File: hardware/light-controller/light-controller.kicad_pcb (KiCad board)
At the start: 2 copper layers, 73 x 35 mm, 124 parts, among them J1 BATT 4S-6S, J2 USB-C, J3 SWD, J4 UART to FC, M1 RM2, Q1 DMP6023LE, SW1 BOOTSEL, U1 LMR51420YDDCR, U2 RP2350A, U3 W25Q16JVSNIQ, U4 USBLC6-2SC6, U5 AL8860MP-13, U6 AL8860MP-13, U7 AL8860MP-13, U8 AL8860MP-13, Y1 12MHz

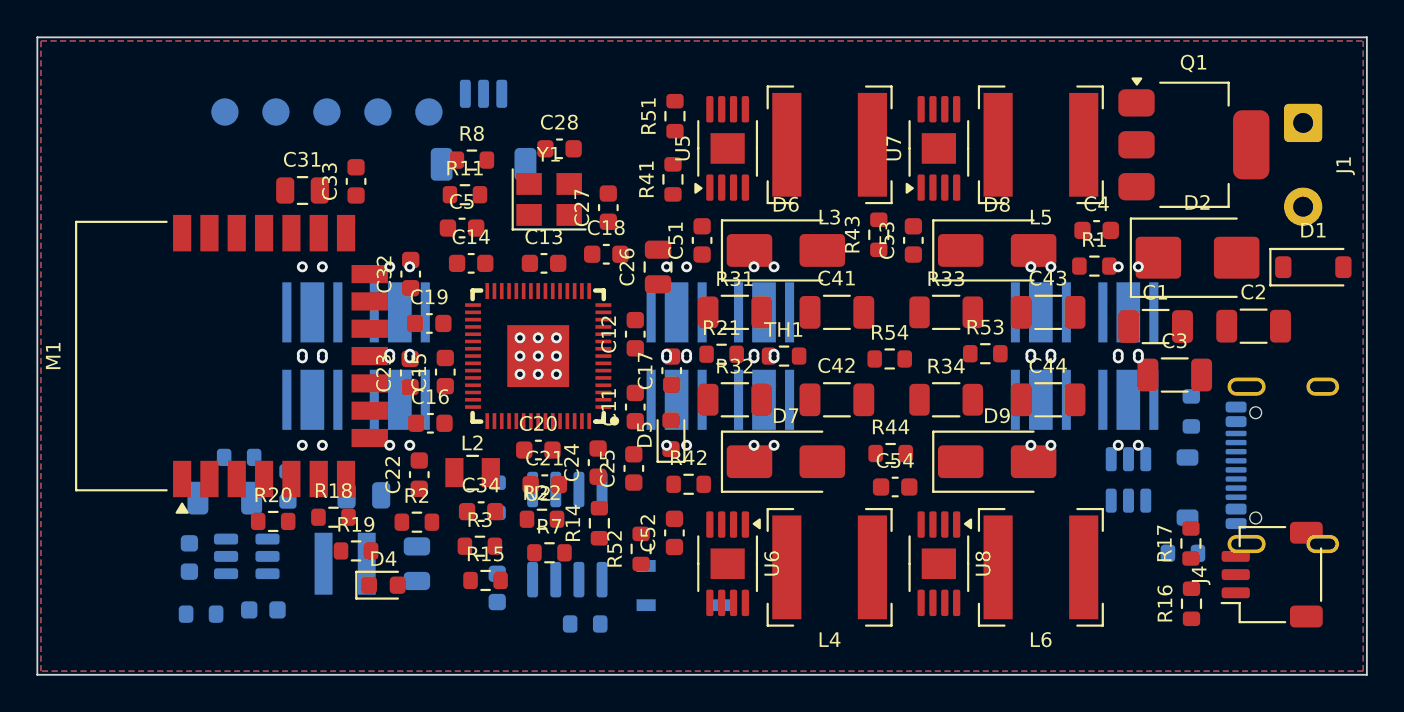
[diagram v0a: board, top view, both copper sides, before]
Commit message: light-controller: LED array per colour row, no USB, routing tools, README (WIP)
Co-Authored-By: Claude Opus 5.5 (1M context) <noreply@anthropic.com>
Claude-Session: https://claude.ai/code/session_01KXRTPSv3xMSgDNs8D9aXZS
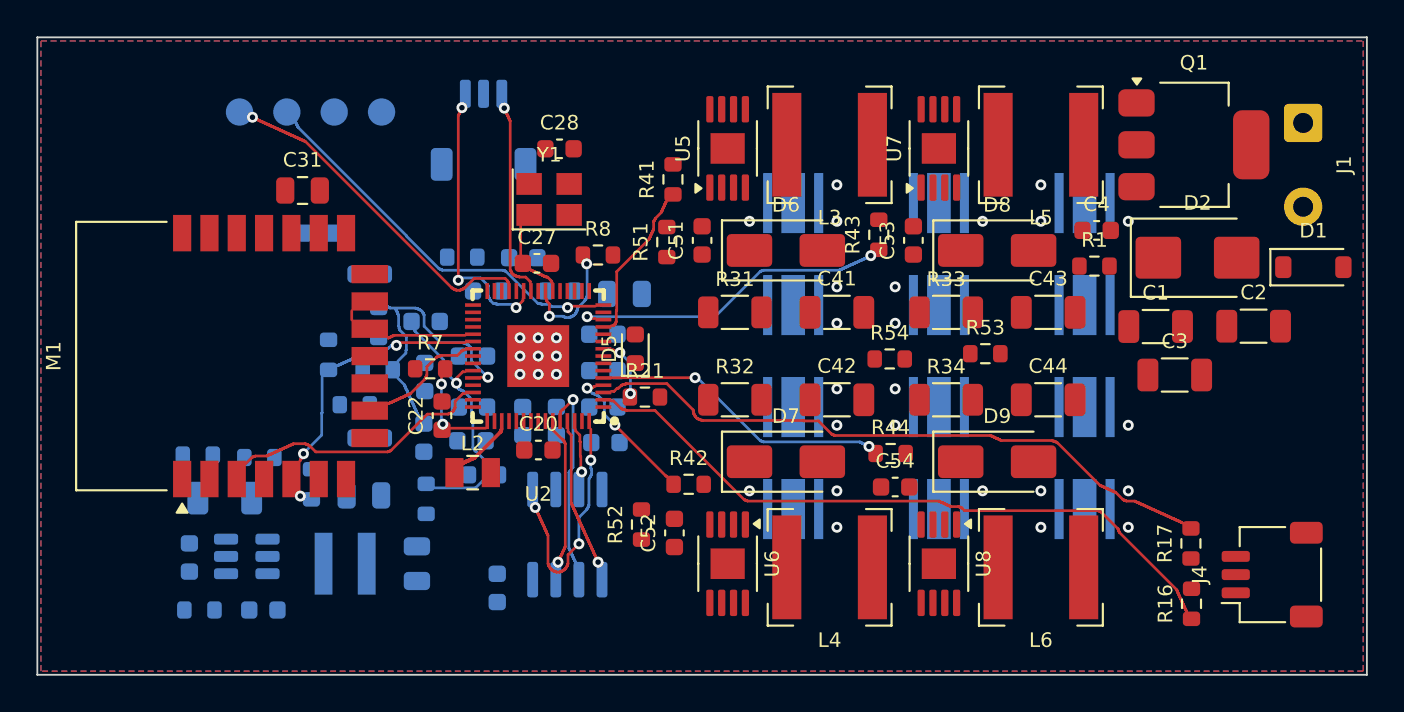
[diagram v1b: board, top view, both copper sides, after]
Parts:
- removed D3: B5819W, lightctl:D_SOD-123
- removed J2: USB-C, lightctl:USB_C_Receptacle_GCT_USB4105-xx-A_16P_TopMnt_Horizontal
- removed R10: 1k, lightctl:R_0603_1608Metric
- removed R12, R13: 5.1k, lightctl:R_0603_1608Metric
- removed R14, R15: 27, lightctl:R_0603_1608Metric
- removed R9: 10k, lightctl:R_0603_1608Metric
- removed SW1: BOOTSEL, lightctl:SW_SPST_PTS810
- removed TP5: GPIO28, lightctl:TestPoint_Pad_D1.5mm
- removed U4: USBLC6-2SC6, lightctl:SOT-23-6
- C11, C12, C13, C14, C15, C16, C17, C18, C19, C21, C23, C24, C25, C26, C32, C33, C34, C5, D4, R11, R18, R19, R2, R20, R22, R3, TH1: moved to B.Cu
- TP2: value GPIO8 -> GPIO10
- TP3: value GPIO9 -> GPIO11
- moved LED1 27.1 mm to (5.00, -8.40), turned to 180 degrees
- moved LED7 26.9 mm to (5.00, -2.80), turned to 180 degrees
- moved LED10 22.4 mm to (5.00, 8.40), turned to 180 degrees
- moved LED4 22.2 mm to (5.00, 2.80), turned to 180 degrees
- moved TH1 21.2 mm to (-15.2, 7.84), turned to -90 degrees
- moved LED2 15.6 mm to (13.0, -8.40), turned to 180 degrees
- moved LED8 15.3 mm to (13.0, -2.80), turned to 180 degrees
- moved R3 13.5 mm to (-17.8, -1.82), turned to -90 degrees
- moved R7 12.0 mm to (-14.9, 0.70)
- moved C5 11.7 mm to (-15.3, 4.48), turned to -90 degrees
- moved LED11 11.3 mm to (13.0, 8.40), turned to 180 degrees
- moved LED5 10.9 mm to (13.0, 2.80), turned to 180 degrees
- moved C34 10.9 mm to (-15.2, -1.90)
- moved R20 9.64 mm to (-20.5, -0.07), turned to -90 degrees
- moved R6 8.74 mm to (-27.7, 5.43)
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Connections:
- TP2 pad 1: /GPIO8 -> /GPIO10
- TP3 pad 1: /GPIO9 -> /GPIO11
- U2 pad 12: /GPIO8 -> /PWM_R
- U2 pad 13: /GPIO9 -> /PWM_B
- U2 pad 14: unconnected-(U2-GPIO10-Pad14) -> /GPIO10
- U2 pad 15: unconnected-(U2-GPIO11-Pad15) -> /GPIO11
- U2 pad 4: /PWM_R -> /PWM_G
- U2 pad 42: /GPIO28 -> unconnected-(U2-GPIO28_ADC2-Pad42)
- U2 pad 5: /PWM_G -> /PWM_W
- U2 pad 51: /USB_DM -> unconnected-(U2-USB_DM-Pad51)
- U2 pad 52: /USB_DP -> unconnected-(U2-USB_DP-Pad52)
- U2 pad 7: /PWM_B -> unconnected-(U2-GPIO4-Pad7)
- U2 pad 8: /PWM_W -> unconnected-(U2-GPIO5-Pad8)
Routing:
- net /UART_TX: track 0.00 -> 36.8 mm
- net /UART_RX: track 0.00 -> 34.9 mm
- net /GPIO11: track 0.00 -> 20.8 mm, vias 0 -> 1
- net /GPIO16: track 0.00 -> 18.4 mm, vias 0 -> 1
- net /PWM_B: track 0.00 -> 17.5 mm, vias 0 -> 2
- net /PWM_W: track 0.00 -> 15.7 mm, vias 0 -> 2
- net /SWDIO: track 0.00 -> 14.5 mm, vias 0 -> 3
- net /WL_CLK: track 0.00 -> 14.3 mm
- net /VBAT_SENSE: track 0.00 -> 14.1 mm, vias 0 -> 1
- net /NTC_SENSE: track 0.00 -> 13.4 mm, vias 2 -> 1
- net /QSPI_SS: track 0.00 -> 13.0 mm, vias 0 -> 3
- net /WL_D: track 0.00 -> 12.8 mm, vias 0 -> 3
- net /SWCLK: track 0.00 -> 10.5 mm, vias 0 -> 1
- net /QSPI_SCLK: track 0.00 -> 10.2 mm, vias 0 -> 1
- net /PWM_R: track 0.00 -> 8.15 mm
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
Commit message: light-controller: finish routing, pass DRC, add fab outputs
All nets routed on 2 layers with 0 DRC errors against the PCBWay rules
(silkscreen warnings only). Ground islands are stitched to the main pour,
leftover rip-up stubs are removed, and the board netlist matches design.py
pad for pad. Adds the gerber zip, BOM and placement file for PCBWay, fresh
renders, and README notes on DRC, spare pins and the status LED.

Co-Authored-By: Claude Opus 5.5 (1M context) <noreply@anthropic.com>
Claude-Session: https://claude.ai/code/session_01KXRTPSv3xMSgDNs8D9aXZS
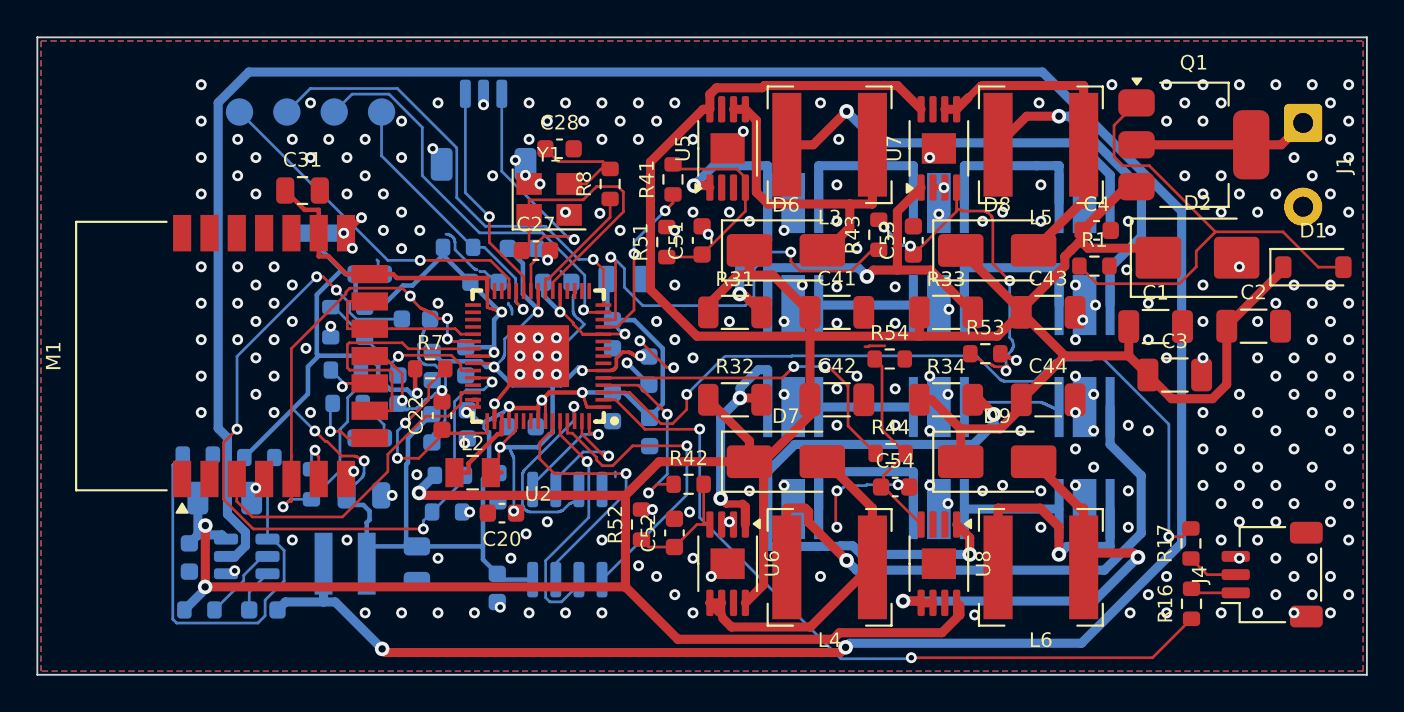
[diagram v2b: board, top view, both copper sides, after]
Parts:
- removed D5: green, lightctl:LED_0603_1608Metric
- removed R21: 1k, lightctl:R_0603_1608Metric
- moved R3 11.0 mm to (-14.0, 8.56), turned to 0 degrees
- moved TH1 11.0 mm to (-20.4, -1.86)
- moved R22 10.6 mm to (-18.5, -1.83), turned to -90 degrees
- moved R2 7.02 mm to (-13.8, 6.55)
- moved C5 6.52 mm to (-15.7, -2.03), turned to 0 degrees
- moved C24 4.85 mm to (-11.2, 7.20)
- moved C34 4.04 mm to (-16.7, 1.84), turned to -90 degrees
- moved C20 4.00 mm to (-11.0, 8.62), turned to 180 degrees
- moved R8 3.96 mm to (-5.05, -9.45), turned to 90 degrees
- moved C17 2.50 mm to (-2.92, 0.80), turned to -90 degrees
- moved C25 2.50 mm to (-2.88, 4.17), turned to -90 degrees
- moved C23 2.28 mm to (-14.8, 3.97), turned to -90 degrees
- moved R20 1.27 mm to (-19.6, 0.77), turned to 0 degrees
- moved C16 1.00 mm to (-12.9, 3.75), turned to -90 degrees
- moved C26 0.82 mm to (-4.25, -4.23)
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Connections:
- U2 pad 9: /STAT_LED -> unconnected-(U2-GPIO6-Pad9)
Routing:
- net /VIN: track 0.00 -> 212.9 mm, vias 0 -> 3
- net /BUCK_SW: track 0.00 -> 156.8 mm, vias 0 -> 2
- net /+3V3: track 0.00 -> 138.9 mm, vias 0 -> 11
- net /GND: track 0.00 -> 46.2 mm, vias 33 -> 288
- net /+1V1: track 0.00 -> 37.9 mm, vias 0 -> 6
- net /LEDK_G: track 0.00 -> 32.9 mm, vias 0 -> 1
- net /LEDA_W: track 0.00 -> 32.9 mm, vias 0 -> 2
- net /VBAT_SENSE: track 14.1 -> 43.7 mm, vias 1 -> 5
- net /FET_GATE: track 0.00 -> 28.1 mm
- net /SW_W: track 0.00 -> 25.7 mm, vias 0 -> 2
- net /BUCK_FB: track 0.00 -> 24.4 mm
- net /GPIO10: track 0.00 -> 22.9 mm, vias 0 -> 1
- net /LEDK_R: track 0.00 -> 21.5 mm, vias 0 -> 1
- net /LEDA_B: track 0.00 -> 19.7 mm, vias 0 -> 1
- net /CTRL_B: track 0.00 -> 19.7 mm, vias 0 -> 4
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
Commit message: light-controller: vertical SWD connector so the probe plugs in from below
The horizontal JST-SH on the bottom opened toward the middle of the board,
so the probe plug and cable ran into the parts around it, and the long edges
are inside the rail so it can't face outward. J3 is now a BM03B-SRSS-TB
vertical with the signal pads where they were; SWCLK, SWDIO and GPIO11 are
re-routed around it. DRC still 0 errors.

Co-Authored-By: Claude Opus 5.5 (1M context) <noreply@anthropic.com>
Claude-Session: https://claude.ai/code/session_01KXRTPSv3xMSgDNs8D9aXZS
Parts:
- J3: footprint lightctl:JST_SH_SM03B-SRSS-TB_1x03-1MP_P1.00mm_Horizontal -> lightctl:JST_SH_BM03B-SRSS-TB_1x03-1MP_P1.00mm_Vertical
- moved J3 0.67 mm to (-12.0, -13.1), turned to 0 degrees
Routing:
- net /SWDIO: track 12.2 -> 11.1 mm
- net /GPIO11: track 25.6 -> 26.2 mm

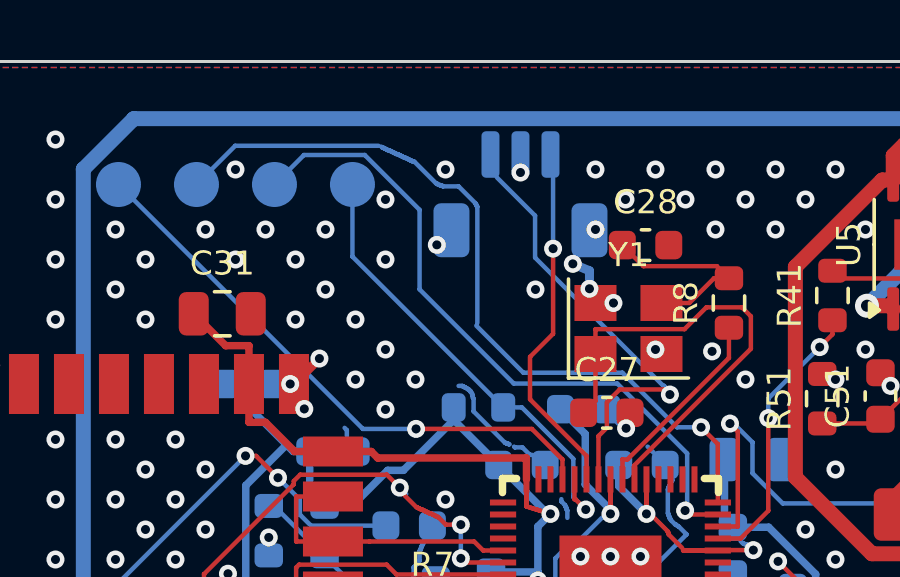
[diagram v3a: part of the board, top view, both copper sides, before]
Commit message: light-controller: drop the SWD connector, program through pogo-pin pads
J3 is gone. SWCLK, GND and SWDIO are now test pads TP5-TP7 in the same
2.6 mm row as RUN and the spare GPIOs, so one pogo jig reaches all seven.
GPIO10/11 and the SWD nets are re-routed around the new pads; DRC is
still 0 errors and the netlist matches design.py.

Co-Authored-By: Claude Opus 5.5 (1M context) <noreply@anthropic.com>
Claude-Session: https://claude.ai/code/session_01KXRTPSv3xMSgDNs8D9aXZS
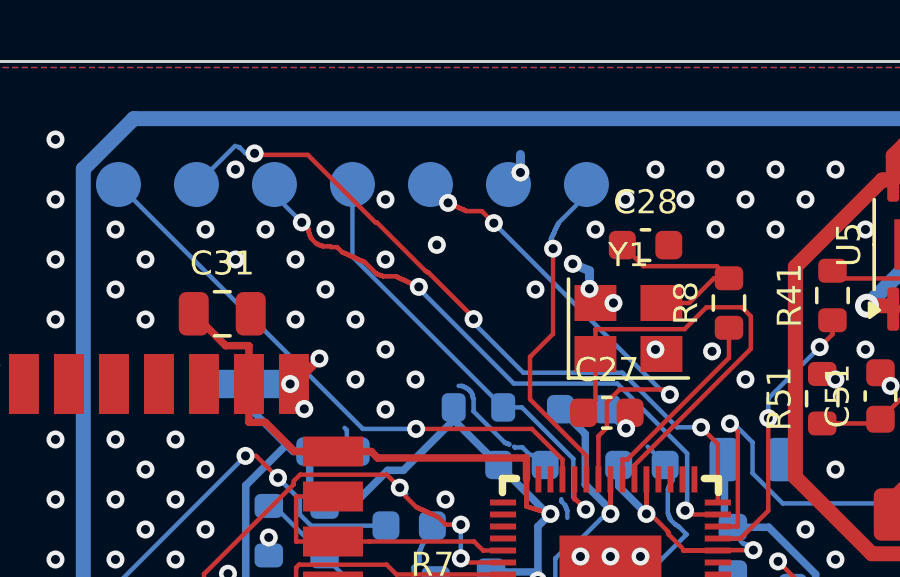
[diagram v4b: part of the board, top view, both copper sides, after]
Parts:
- removed J3: SWD, lightctl:JST_SH_BM03B-SRSS-TB_1x03-1MP_P1.00mm_Vertical
- added TP5: SWCLK, lightctl:TestPoint_Pad_D1.5mm, B.Cu at (-15.0, -13.4)
- added TP6: GND, lightctl:TestPoint_Pad_D1.5mm, B.Cu at (-12.4, -13.4)
- added TP7: SWDIO, lightctl:TestPoint_Pad_D1.5mm, B.Cu at (-9.80, -13.4)
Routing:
- net /GPIO10: track 22.9 -> 20.0 mm, vias 1 -> 3
- net /GPIO11: track 26.2 -> 23.9 mm, vias 1 -> 3
- net /SWDIO: track 11.1 -> 10.3 mm
- net /SWCLK: track 14.3 -> 14.8 mm, vias 1 -> 3
- net /GND: vias 288 -> 286
